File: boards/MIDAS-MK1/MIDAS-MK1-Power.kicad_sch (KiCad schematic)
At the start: 43 parts, among them U1 TI_TPS566242DRLR, U2 TI_TPS566242DRLR, U5 TPS2121RUXR

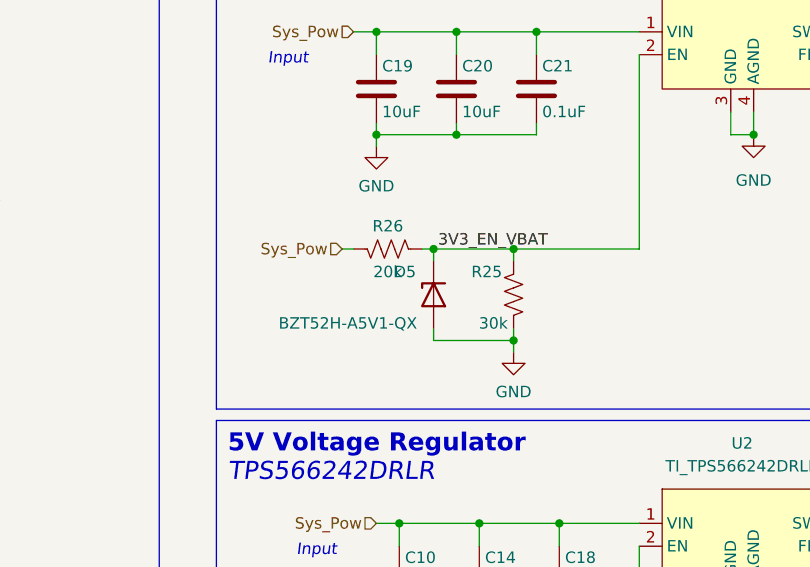
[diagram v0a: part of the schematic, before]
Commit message: adjusting placement and labels
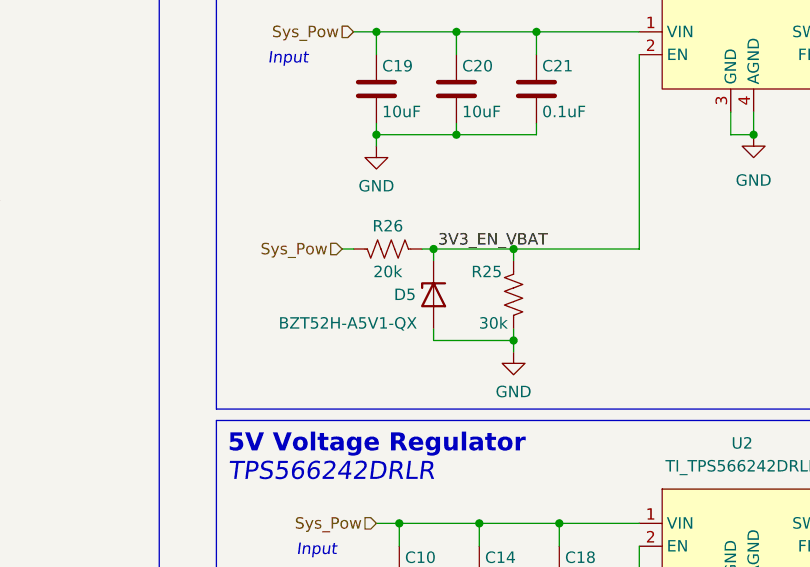
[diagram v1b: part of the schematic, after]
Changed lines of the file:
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@@
   (symbol (lib_id "Device:D_Zener") (at 241.3 138.43 90) (mirror x) (unit 1)
     (in_bom yes) (on_board yes) (dnp no)
-    (property "Reference" "D5" (at 238.125 135.89 90)
+    (property "Reference" "D5" (at 238.125 138.43 90)
       (effects (font (size 1.27 1.27)))
     )

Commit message: general improvements
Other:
- moved on the sheet: C10, C12, C14, C16, C18, C19, C20, C21, C22, C23, C24, C25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

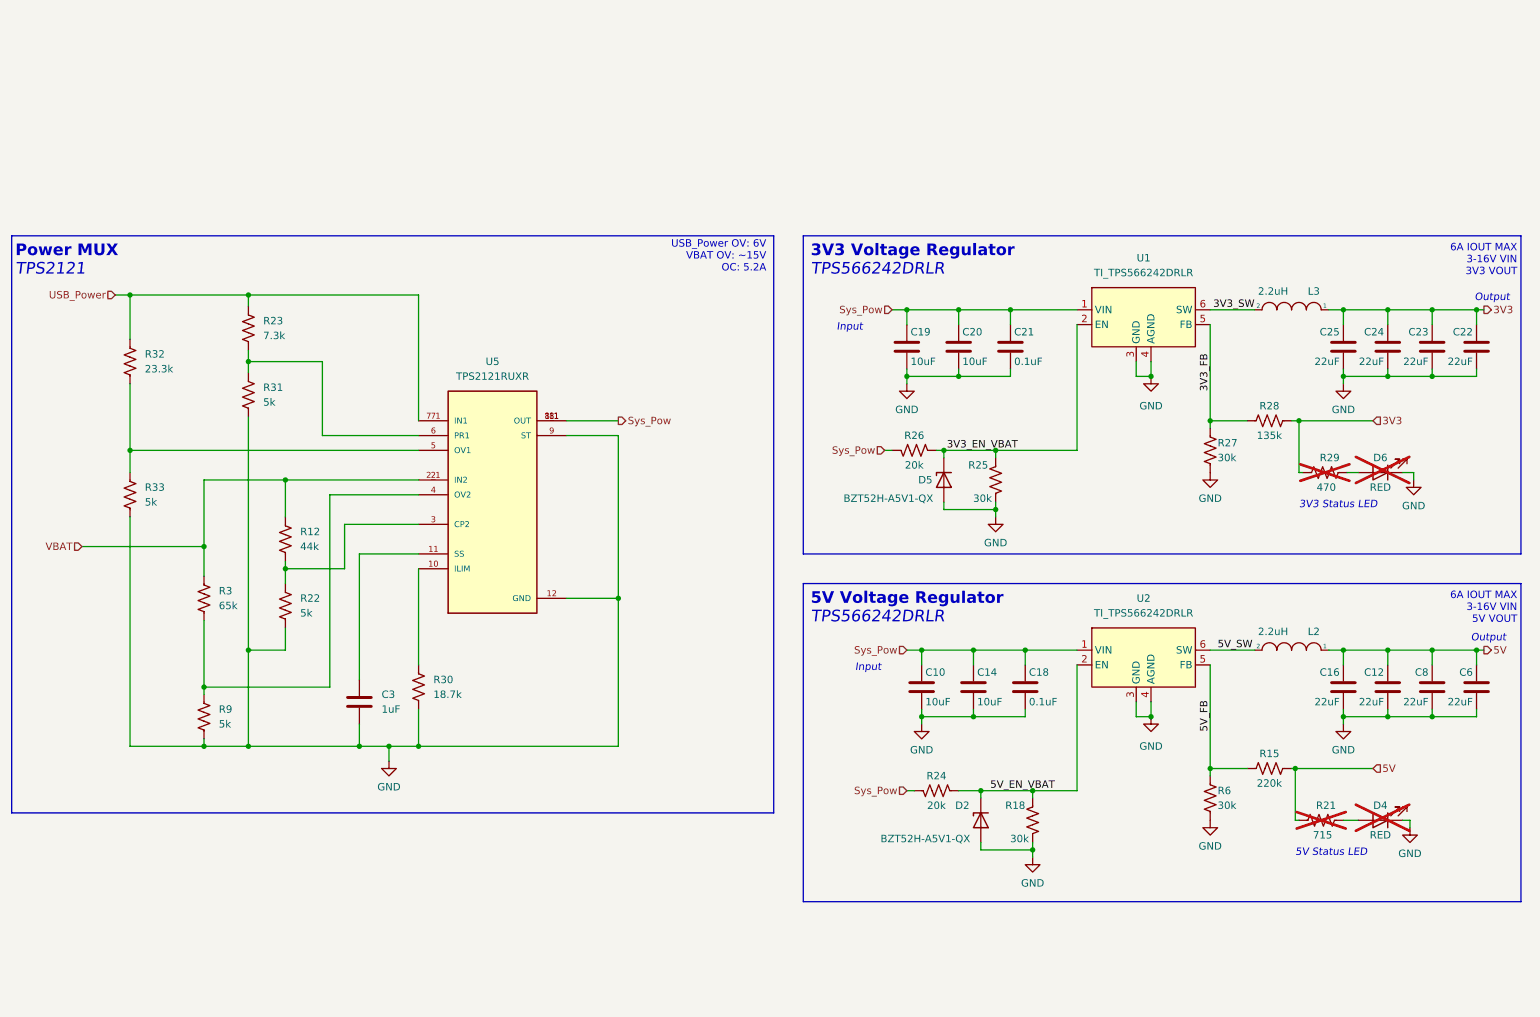
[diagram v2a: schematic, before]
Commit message: Added new symbols with correct fps, need to connect
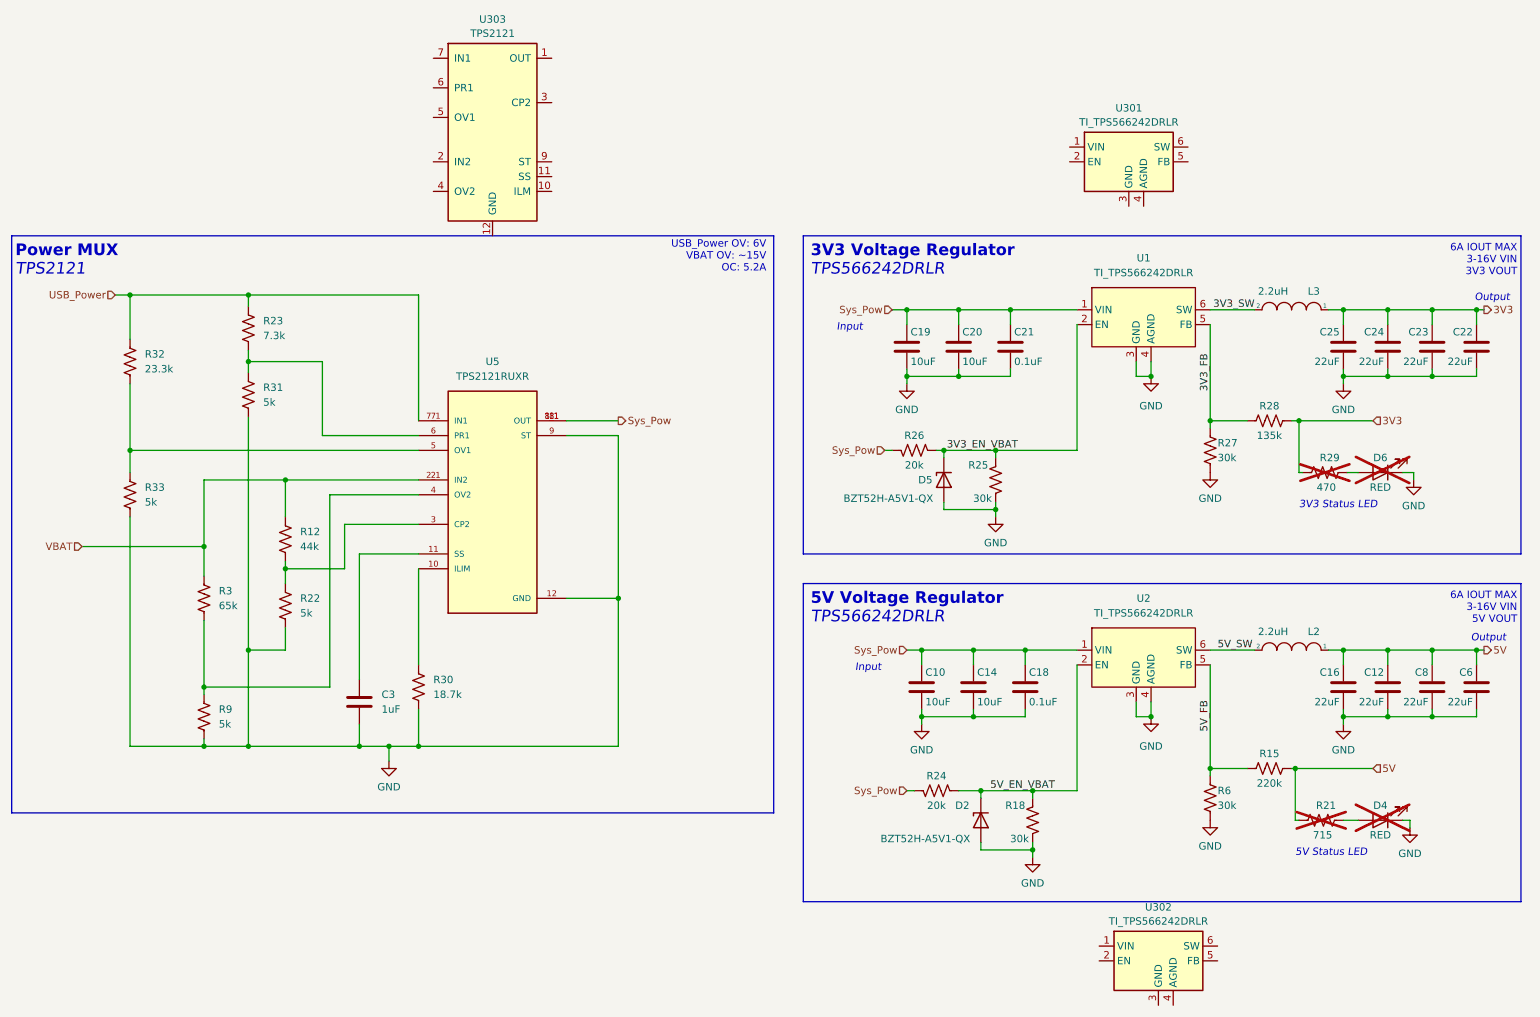
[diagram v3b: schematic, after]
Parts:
- added U301, U302: TI_TPS566242DRLR, Package_TO_SOT_SMD:SOT-563, symbol Regulator_Texas:TI_TPS566242DRLR
- added U303: TPS2121, Package_VQFN:VQFN-HR-RUX0012A, symbol Power_MUX:TPS2121
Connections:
- new net: U303.1 (OUT), U303.8 (OUT)
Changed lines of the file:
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@@
+    )
+  )
+  (symbol (lib_id "Power_MUX:TPS2121") (at 162.56 78.74 0) (unit 1)
+    (in_bom yes) (on_board yes) (dnp no) (fields_autoplaced)
+    (property "Reference" "U303" (at 162.56 59.3557 0)
+      (effects (font (size 1.27 1.27)))
+    )
+    (property "Value" "TPS2121" (at 162.56 61.7799 0)
+      (effects (font (size 1.27 1.27)))
+    )
+    (property "Footprint" "Package_VQFN:VQFN-HR-RUX0012A" (at 162.56 78.74 0)
+      (effects (font (size 1.27 1.27)) (justify bottom) hide)
+    )
+    (property "Datasheet" "https://www.ti.com/product/TPS2121" (at 162.56 78.74 0)
+      (effects (font (size 1.27 1.27)) hide)
+    )
+    (pin "10")
+    (pin "11")
+    (pin "12")
+    (pin "2")
+    (pin "3")
+    (pin "4")
+    (pin "5")
+    (pin "6")
+    (pin "7")
+    (pin "9")
+    (pin "1")
+    (pin "8")
+    (instances
+      (project "MIDAS-MK1"
+        (path "/6007cf46-4651-4a02-8f98-d5846f3575c7/6a3d8d20-17ea-4f21-96e4-14cd4e641450"
+          (reference "U303") (unit 1)
+        )
+      )
     )
   )
@@
         (path "/e63e39d7-6ac0-4ffd-8aa3-1841a4541b55"
           (reference "L101") (unit 1)
+        )
+      )
+    )
+  )
+  (symbol (lib_name "TI_TPS566242DRLR_1") (lib_id "Regulator_Texas:TI_TPS566242DRLR") (at 276.86 220.98 0) (unit 1)
+    (in_bom yes) (on_board yes) (dnp no) (fields_autoplaced)
+    (property "Reference" "U302" (at 276.86 211.7557 0)
+      (effects (font (size 1.27 1.27)))
+    )
+    (property "Value" "TI_TPS566242DRLR" (at 276.86 214.1799 0)
+      (effects (font (size 1.27 1.27)))
+    )
+    (property "Footprint" "Package_TO_SOT_SMD:SOT-563" (at 276.86 220.98 0)
+      (effects (font (size 1.27 1.27)) hide)
+    )
+    (property "Datasheet" "https://www.ti.com/lit/ds/symlink/tps566242.pdf" (at 276.86 220.98 0)
+      (effects (font (size 1.27 1.27)) hide)
+    )
+    (pin "1")
+    (pin "3")
+    (pin "4")
+    (pin "2")
+    (pin "5")
+    (pin "6")
+    (instances
+      (project "MIDAS-MK1"
+        (path "/6007cf46-4651-4a02-8f98-d5846f3575c7/6a3d8d20-17ea-4f21-96e4-14cd4e641450"
+          (reference "U302") (unit 1)
         )
       )
@@
         )
       )
+    )
+  )
+  (symbol (lib_name "TI_TPS566242DRLR_1") (lib_id "Regulator_Texas:TI_TPS566242DRLR") (at 271.78 83.82 0) (unit 1)
+    (in_bom yes) (on_board yes) (dnp no) (fields_autoplaced)
+    (property "Reference" "U301" (at 271.78 74.5957 0)
+      (effects (font (size 1.27 1.27)))
+    )
+    (property "Value" "TI_TPS566242DRLR" (at 271.78 77.0199 0)
+      (effects (font (size 1.27 1.27)))
+    )
+    (property "Footprint" "Package_TO_SOT_SMD:SOT-563" (at 271.78 83.82 0)
+      (effects (font (size 1.27 1.27)) hide)
+    )
+    (property "Datasheet" "https://www.ti.com/lit/ds/symlink/tps566242.pdf" (at 271.78 83.82 0)
+      (effects (font (size 1.27 1.27)) hide)
+    )
+    (pin "1")
+    (pin "3")
+    (pin "4")
+    (pin "2")
+    (pin "5")
+    (pin "6")
+    (instances
+      (project "MIDAS-MK1"
+        (path "/6007cf46-4651-4a02-8f98-d5846f3575c7/6a3d8d20-17ea-4f21-96e4-14cd4e641450"
+          (reference "U301") (unit 1)
+        )
+      )

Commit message: Updated sch to have new libs
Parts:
- renumbered C3 to C301, C19 to C302, C10 to C303, C20 to C304, C14 to C305, C21 to C306, C18 to C307, C25 to C308, C16 to C309, C24 to C310, C12 to C311, C23 to C312, C8 to C313, C22 to C314, C6 to C315, D5 to D301, D2 to D302, D6 to D303, D4 to D304, L3 to L301, L2 to L302, R32 to R301, R33 to R302, R3 to R303, R9 to R304, R23 to R305, R31 to R306, R12 to R307, R22 to R308, R30 to R309, R26 to R310, R24 to R311, R25 to R312, R18 to R313, R27 to R314, R6 to R315, R28 to R316, R15 to R317, R21 to R318, R29 to R319, U303 to U301, U5 to U302, U301 to U303, U1 to U304, U2 to U305, U302 to U306

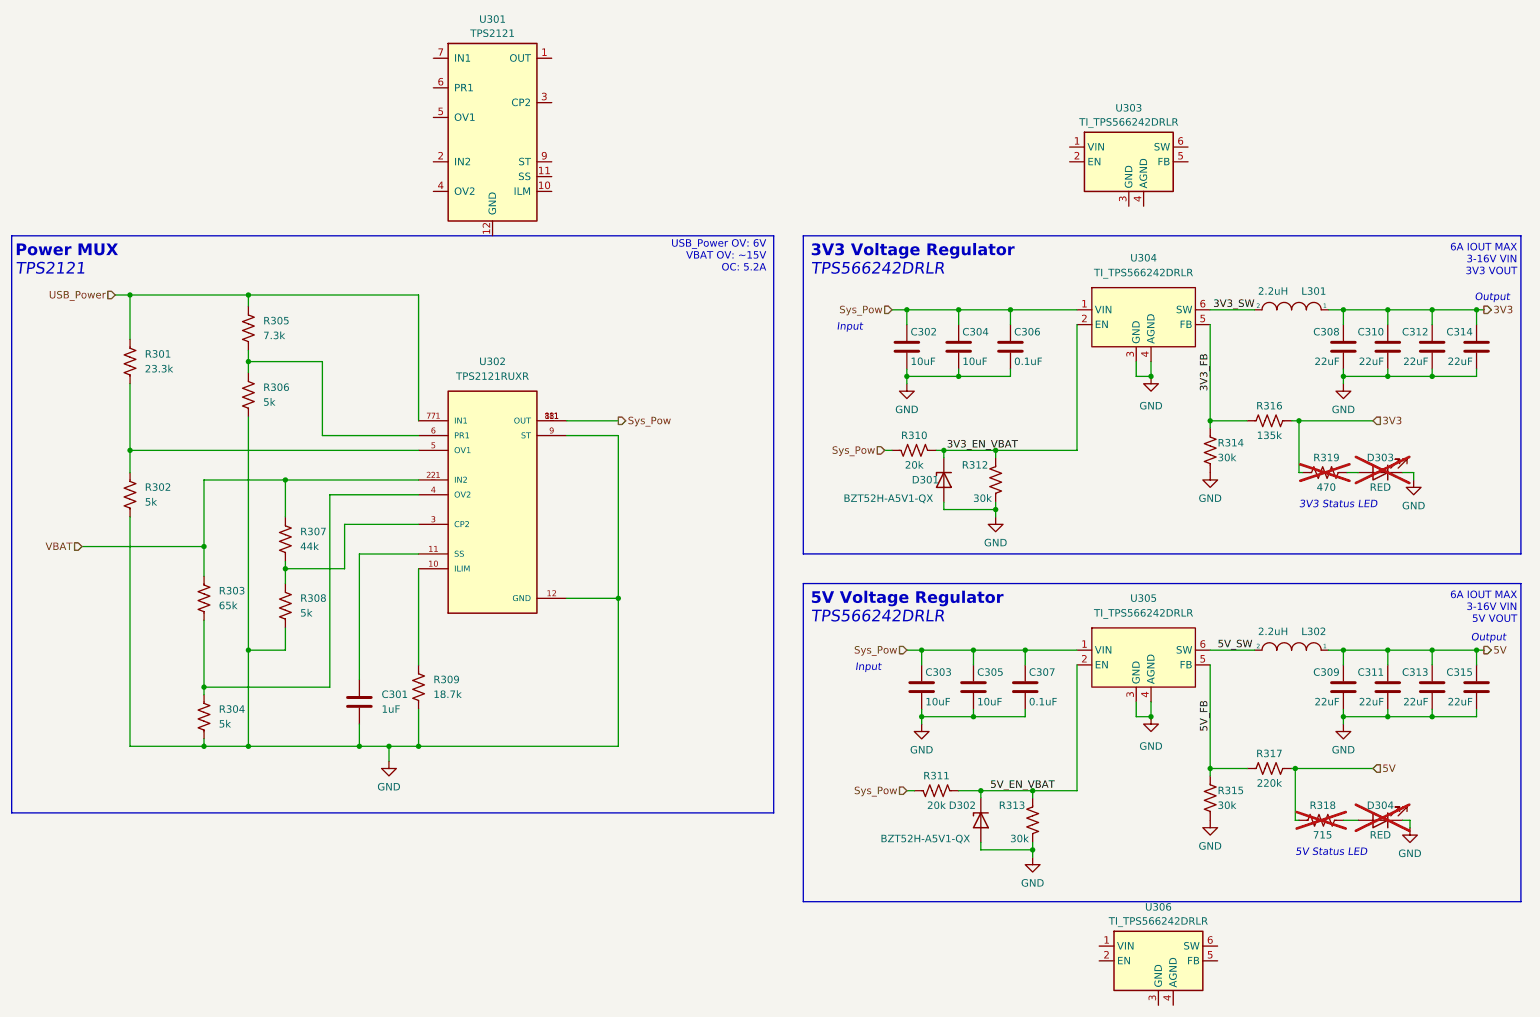
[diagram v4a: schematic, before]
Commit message: reworked power sch
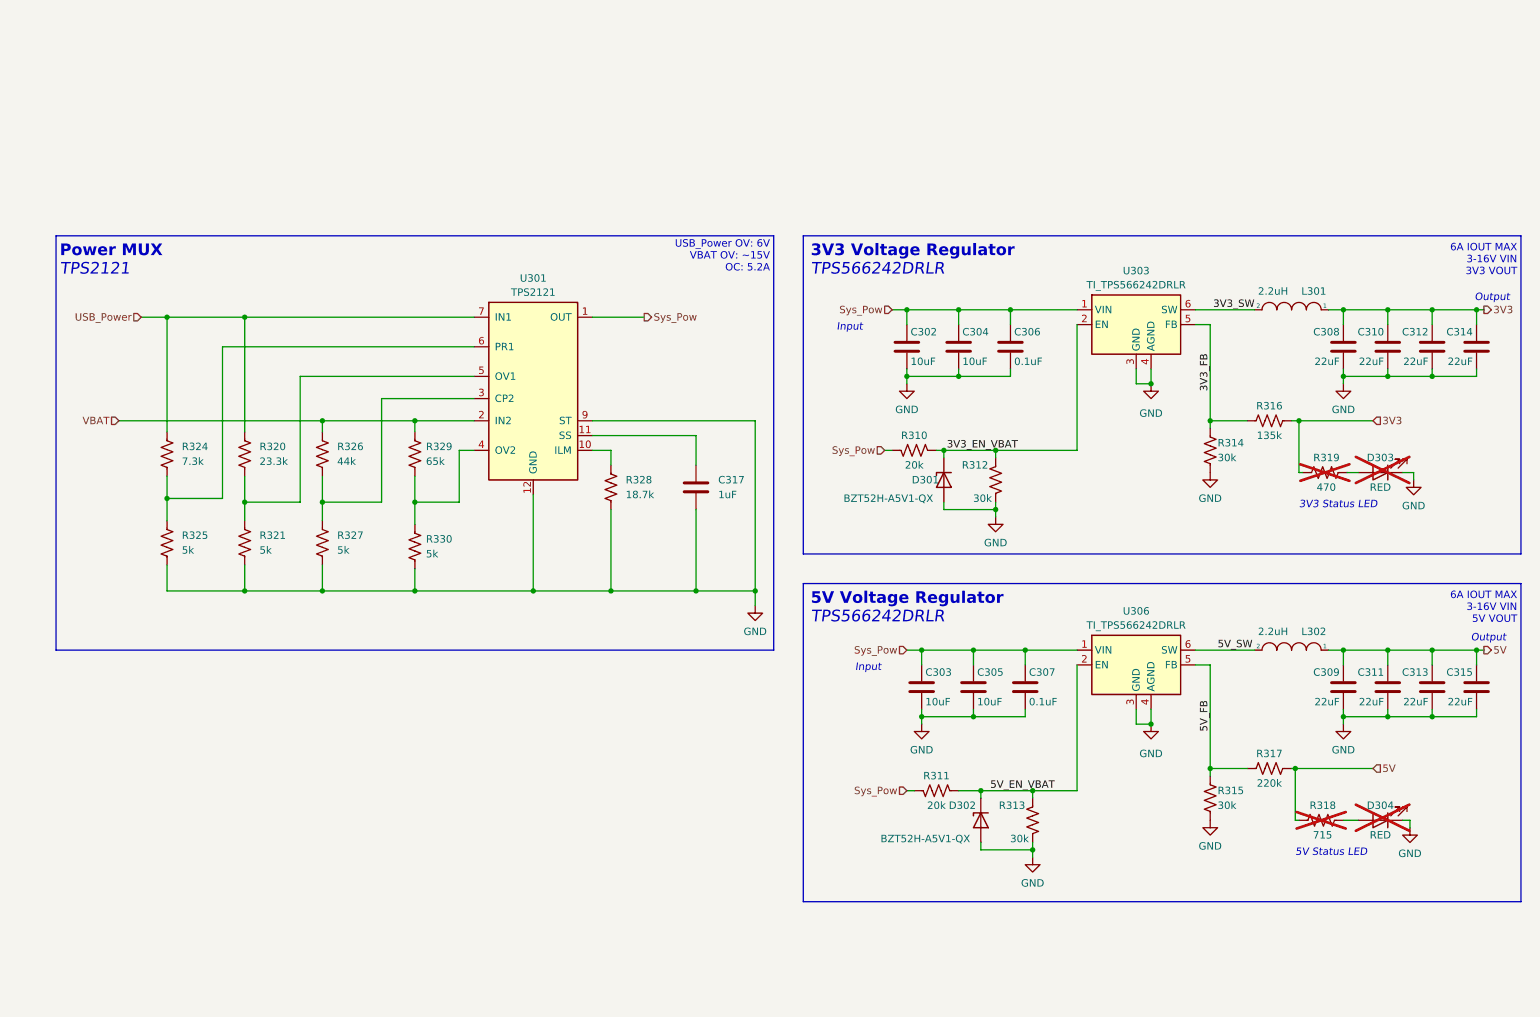
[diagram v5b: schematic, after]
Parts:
- removed C301: 1uF, Capacitor_SMD:C_0603_1608Metric, symbol Device:C
- removed R301: 23.3k, Resistor_SMD:R_0603_1608Metric, symbol Device:R_US
- removed R302, R304, R306, R308: 5k, Resistor_SMD:R_0603_1608Metric, symbol Device:R_US
- removed R303: 65k, Resistor_SMD:R_0603_1608Metric, symbol Device:R_US
- removed R305: 7.3k, Resistor_SMD:R_0603_1608Metric, symbol Device:R_US
- removed R307: 44k, Resistor_SMD:R_0603_1608Metric, symbol Device:R_US
- removed R309: 18.7k, Resistor_SMD:R_0603_1608Metric, symbol Device:R_US
- removed U302: TPS2121RUXR, TPS2121RUXR:IC_TPS2121RUXR, symbol TPS2121RUXR:TPS2121RUXR
- removed U304, U305: TI_TPS566242DRLR, Package_TO_SOT_SMD:SOT-563, symbol Regulator_Texas:TI_TPS566242DRLR
- added C317: 1uF, Capacitor_SMD:C_0603_1608Metric, symbol Device:C
- added R320: 23.3k, Resistor_SMD:R_0603_1608Metric, symbol Device:R_US
- added R321, R325, R327, R330: 5k, Resistor_SMD:R_0603_1608Metric, symbol Device:R_US
- added R324: 7.3k, Resistor_SMD:R_0603_1608Metric, symbol Device:R_US
- added R326: 44k, Resistor_SMD:R_0603_1608Metric, symbol Device:R_US
- added R328: 18.7k, Resistor_SMD:R_0603_1608Metric, symbol Device:R_US
- added R329: 65k, Resistor_SMD:R_0603_1608Metric, symbol Device:R_US
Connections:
- net 3V3_EN_VBAT: now also U303.2 (EN)
- net 3V3_FB: now also U303.5 (FB)
- net 3V3_SW: now also U303.6 (SW)
- net 5V_EN_VBAT: now also U306.2 (EN)
- net 5V_FB: now also U306.5 (FB)
- net 5V_SW: now also U306.6 (SW)
- net GND: now also U301.12 (GND), U301.9 (ST), U303.3 (GND), U303.4 (AGND), U306.3 (GND), U306.4 (AGND), C317.1, R321.2, R325.2, R327.2, R328.1, R330.2
- net Sys_Pow: now also U301.1 (OUT), U301.8 (OUT), U303.1 (VIN), U306.1 (VIN)
- net USB_Power: now also U301.7 (IN1), R320.1, R324.1
- net VBAT: now also U301.2 (IN2), R326.1, R329.1
- net at U301.10 (ILM): now also R328.2
- net at U301.11 (SS): now also C317.2
- net at U301.3 (CP2): now also R326.2, R327.1
- net at U301.4 (OV2): now also R329.2, R330.1
- net at U301.5 (OV1): now also R320.2, R321.1
- net at U301.6 (PR1): now also R324.2, R325.1
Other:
- moved on the sheet: U301, U303, U306
